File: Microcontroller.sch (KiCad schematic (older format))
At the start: 28 parts, among them J1 USB, K1 CONN_3, K2 CONN_3, P23 CONN_1, U3 PIC18F4550, U4 FT230X, X1 4MHz

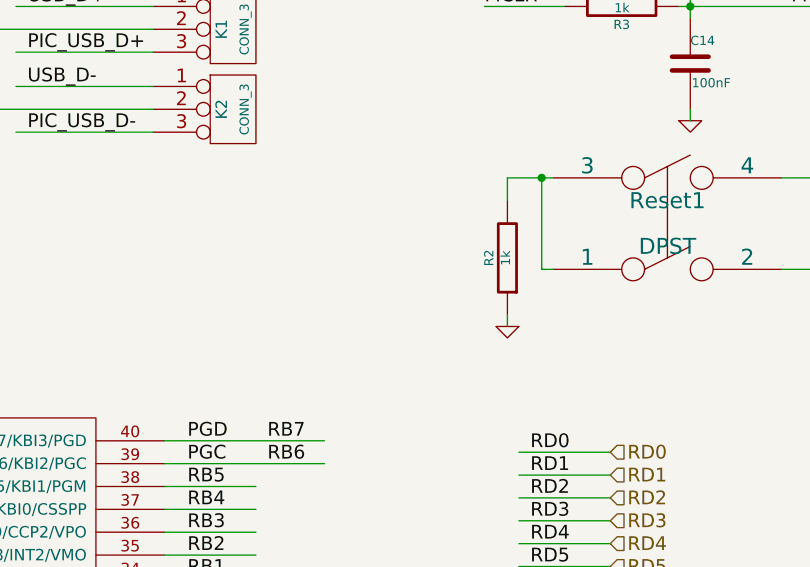
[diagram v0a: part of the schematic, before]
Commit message: Replace resistor R2 with a 0Ohm
Signed-off-by: Kolijn Wolfaardt <kolijn.wolfaardt@gmail.com>
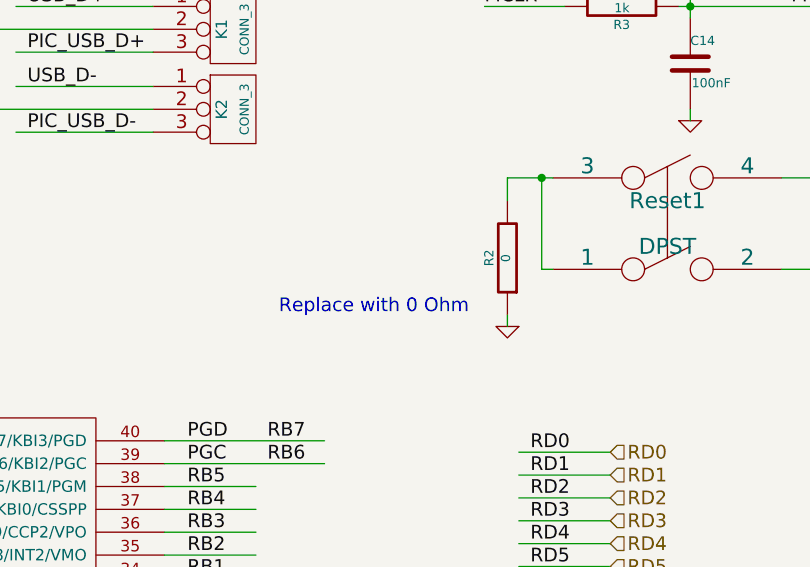
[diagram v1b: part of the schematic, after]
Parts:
- R2: value 1k -> 0
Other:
- note added: "Replace with 0 Ohm"
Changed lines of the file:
@@
 Sheet 4 6
 Title ""
-Date "20 apr 2014"
+Date "20 jul 2014"
 Rev ""
 Comp ""
@@
 P 9050 2600
 F 0 "R2" V 9130 2600 40  0000 C CNN
-F 1 "1k" V 9057 2601 40  0000 C CNN
+F 1 "0" V 9057 2601 40  0000 C CNN
 F 2 "~" V 8980 2600 30  0000 C CNN
 F 3 "~" H 9050 2600 30  0000 C CNN
@@
 	1    0    0    -1
 $EndComp
+Text Notes 8050 2850 0    60   ~ 0
+Replace with 0 Ohm
 $EndSCHEMATC
